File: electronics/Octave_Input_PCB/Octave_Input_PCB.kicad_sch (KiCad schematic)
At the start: 35 parts, among them SW1 SW_Hot_Swap_Socket, SW10 SW_Hot_Swap_Socket, SW11 SW_Hot_Swap_Socket, SW12 SW_Hot_Swap_Socket, SW13 Bourns_PEC12R-4xxxF-Sxxx, SW14 SW_Hot_Swap_Socket, SW2 SW_Hot_Swap_Socket, SW3 SW_Hot_Swap_Socket, SW4 SW_Hot_Swap_Socket, SW5 SW_Hot_Swap_Socket, SW6 SW_Hot_Swap_Socket, SW7 SW_Hot_Swap_Socket, SW8 SW_Hot_Swap_Socket, SW9 SW_Hot_Swap_Socket, U1 Adafruit_QT_Py_RP2040

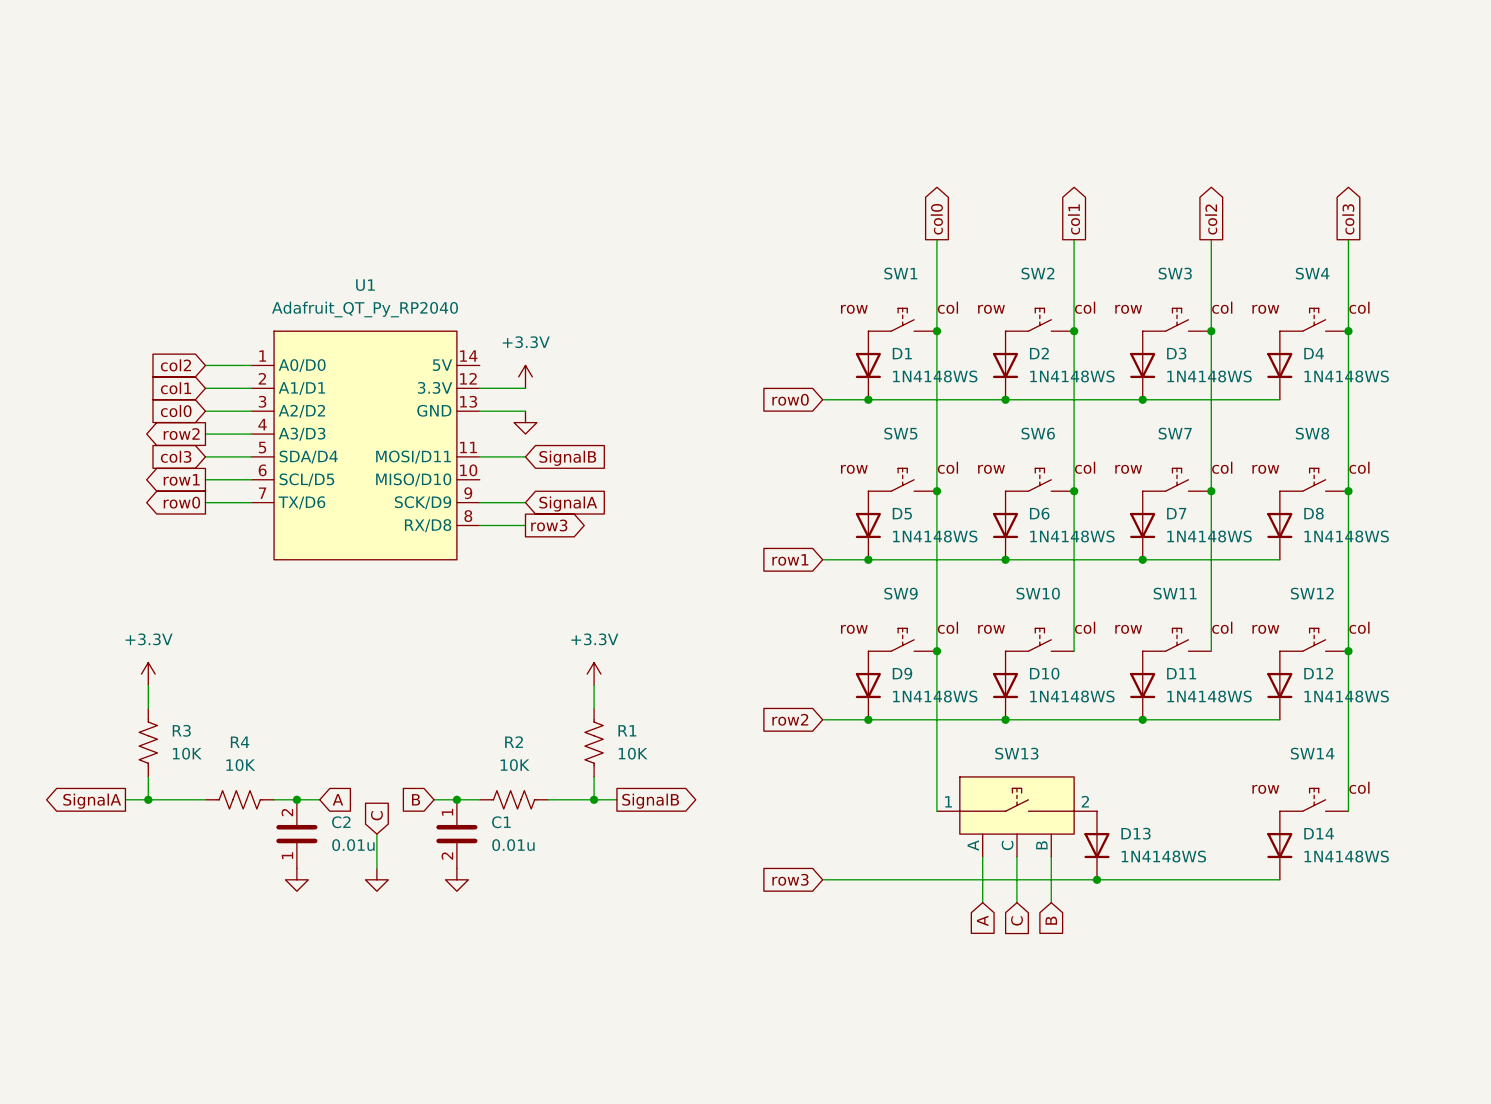
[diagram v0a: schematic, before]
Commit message: Schematic rev.1 is available
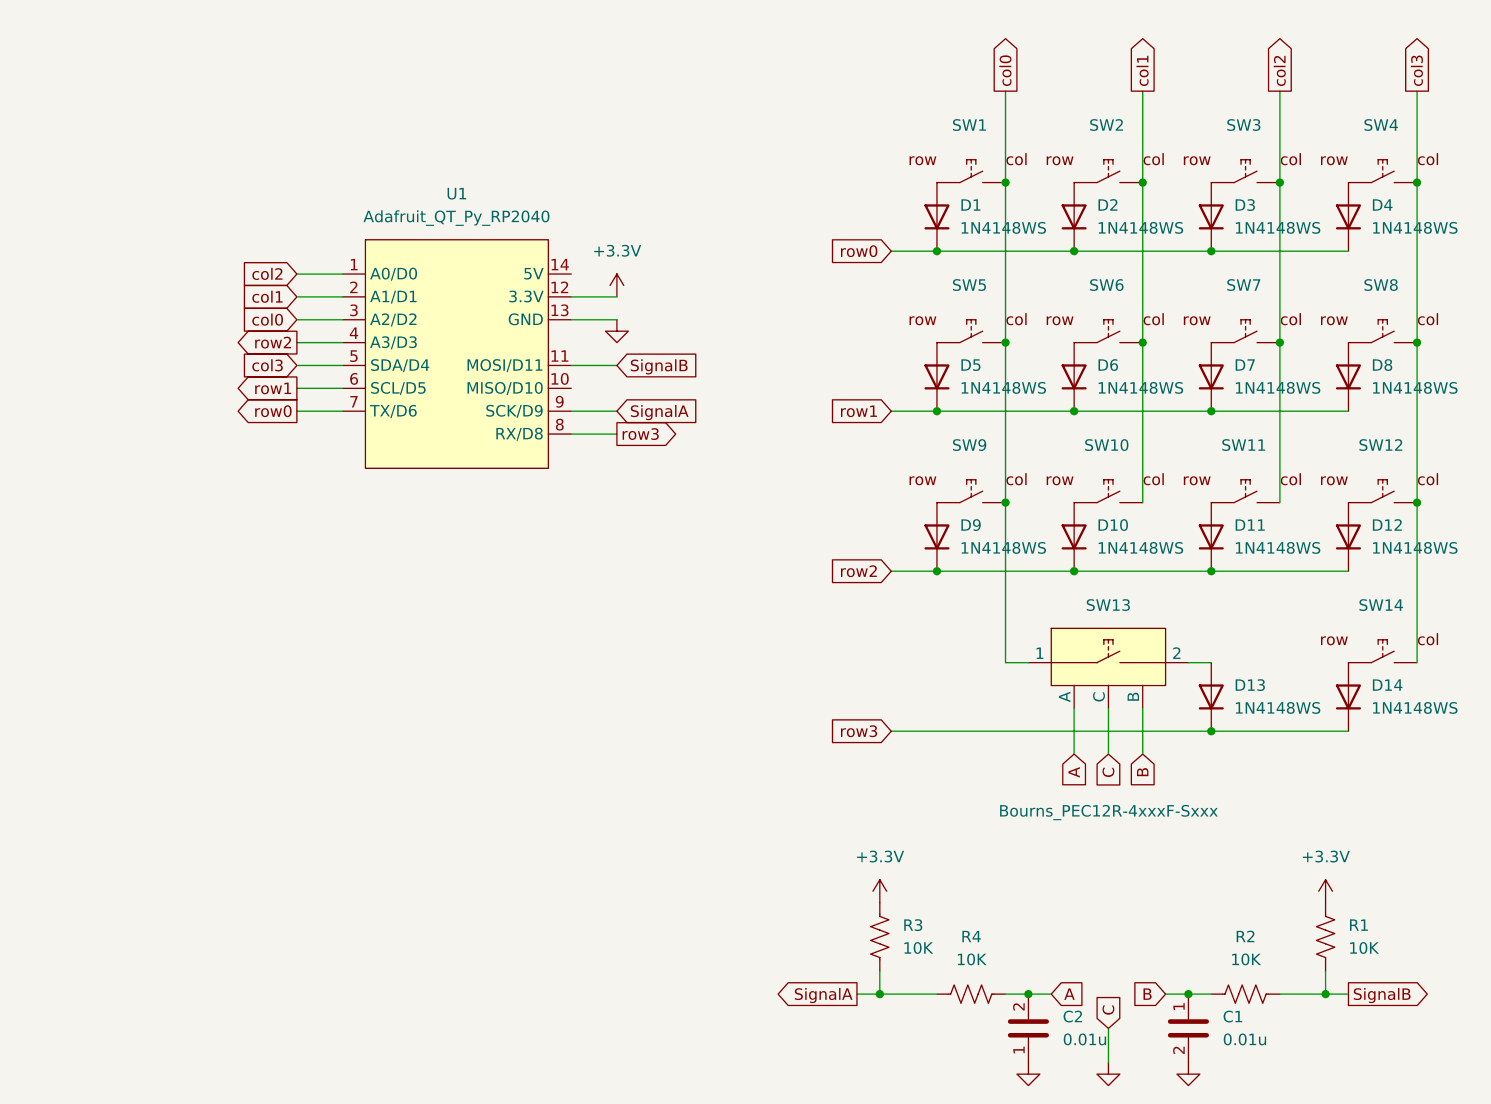
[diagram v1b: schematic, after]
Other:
- title: (none) -> Octave - Input PCB
- moved on the sheet: C1, C2, D1, D10, D11, D12, D13, D14, D2, D3, D4, D5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

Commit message: Reset PCB tracks
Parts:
- C1, C2: footprint Octave_Library:C_0805_2012Metric_Pad1.18x1.45mm_HandSolder -> Octave_Library:C_0805_2012Metric
- R1, R2, R3, R4: footprint Octave_Library:R_0805_2012Metric_Pad1.20x1.40mm_HandSolder -> Octave_Library:R_0805_2012Metric
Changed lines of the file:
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@@
       (effects (font (size 1.27 1.27)) (justify left))
     )
-    (property "Footprint" "Octave_Library:C_0805_2012Metric_Pad1.18x1.45mm_HandSolder" (id 2) (at 183.8452 143.51 0)
+    (property "Footprint" "Octave_Library:C_0805_2012Metric" (id 2) (at 183.8452 143.51 0)
       (effects (font (size 1.27 1.27)) hide)
     )
@@
       (effects (font (size 1.27 1.27)) (justify right))
     )
-    (property "Footprint" "Octave_Library:C_0805_2012Metric_Pad1.18x1.45mm_HandSolder" (id 2) (at 164.1348 135.89 0)
+    (property "Footprint" "Octave_Library:C_0805_2012Metric" (id 2) (at 164.1348 135.89 0)
       (effects (font (size 1.27 1.27)) hide)
     )
@@
     (property "Reference" "R2" (id 0) (at 189.23 129.54 90))
     (property "Value" "10K" (id 1) (at 189.23 132.08 90))
-    (property "Footprint" "Octave_Library:R_0805_2012Metric_Pad1.20x1.40mm_HandSolder" (id 2) (at 189.484 134.874 90)
+    (property "Footprint" "Octave_Library:R_0805_2012Metric" (id 2) (at 189.484 134.874 90)
       (effects (font (size 1.27 1.27)) hide)
     )
@@
     (property "Reference" "R4" (id 0) (at 158.75 129.54 90))
     (property "Value" "10K" (id 1) (at 158.75 132.08 90))
-    (property "Footprint" "Octave_Library:R_0805_2012Metric_Pad1.20x1.40mm_HandSolder" (id 2) (at 158.496 136.906 90)
+    (property "Footprint" "Octave_Library:R_0805_2012Metric" (id 2) (at 158.496 136.906 90)
       (effects (font (size 1.27 1.27)) hide)
     )
@@
       (effects (font (size 1.27 1.27)) (justify left))
     )
-    (property "Footprint" "Octave_Library:R_0805_2012Metric_Pad1.20x1.40mm_HandSolder" (id 2) (at 199.136 129.794 90)
+    (property "Footprint" "Octave_Library:R_0805_2012Metric" (id 2) (at 199.136 129.794 90)
       (effects (font (size 1.27 1.27)) hide)
     )
@@
       (effects (font (size 1.27 1.27)) (justify left))
     )
-    (property "Footprint" "Octave_Library:R_0805_2012Metric_Pad1.20x1.40mm_HandSolder" (id 2) (at 149.606 129.794 90)
+    (property "Footprint" "Octave_Library:R_0805_2012Metric" (id 2) (at 149.606 129.794 90)
       (effects (font (size 1.27 1.27)) hide)
     )
@@
     )
     (path "/172c53e1-ff21-4247-8ac3-d08b615ae4b5"
-      (reference "C1") (unit 1) (value "0.01u") (footprint "Octave_Library:C_0805_2012Metric_Pad1.18x1.45mm_HandSolder")
+      (reference "C1") (unit 1) (value "0.01u") (footprint "Octave_Library:C_0805_2012Metric")
     )
     (path "/21ad77bf-5ff1-4e47-a420-889e2c26128b"
-      (reference "C2") (unit 1) (value "0.01u") (footprint "Octave_Library:C_0805_2012Metric_Pad1.18x1.45mm_HandSolder")
+      (reference "C2") (unit 1) (value "0.01u") (footprint "Octave_Library:C_0805_2012Metric")
     )
     (path "/709f02fa-f113-4f34-aada-ad74ed9e0d25"
@@
     )
     (path "/64730bd7-54fc-4aec-9d2c-870b4ea1cdc7"
-      (reference "R1") (unit 1) (value "10K") (footprint "Octave_Library:R_0805_2012Metric_Pad1.20x1.40mm_HandSolder")
+      (reference "R1") (unit 1) (value "10K") (footprint "Octave_Library:R_0805_2012Metric")
     )
     (path "/21cf072e-e65a-4d3b-9444-6c6fd8351885"
-      (reference "R2") (unit 1) (value "10K") (footprint "Octave_Library:R_0805_2012Metric_Pad1.20x1.40mm_HandSolder")
+      (reference "R2") (unit 1) (value "10K") (footprint "Octave_Library:R_0805_2012Metric")
     )
     (path "/7d5f8a5b-f9ef-4146-ac71-a7ec0f7bb1c4"
-      (reference "R3") (unit 1) (value "10K") (footprint "Octave_Library:R_0805_2012Metric_Pad1.20x1.40mm_HandSolder")
+      (reference "R3") (unit 1) (value "10K") (footprint "Octave_Library:R_0805_2012Metric")
     )
     (path "/4c631ef9-ee73-4b0c-aa59-4f071756ed7f"
-      (reference "R4") (unit 1) (value "10K") (footprint "Octave_Library:R_0805_2012Metric_Pad1.20x1.40mm_HandSolder")
+      (reference "R4") (unit 1) (value "10K") (footprint "Octave_Library:R_0805_2012Metric")
     )
     (path "/ec285e65-9c46-4fa7-bf57-be16d5aaed04"

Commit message: Update schematic
Since label C hid GND in the net list, remove label C and simply connect to GND.
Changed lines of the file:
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@@
     (title "Octave - Input PCB")
     (date "2022-03-06")
-    (rev "1")
+    (rev "2")
     (comment 4 "https://github.com/takayoshiotake/octave-12-key-macropad")
   )
@@
   )
   (wire (pts (xy 193.04 63.5) (xy 193.04 81.28))
-    (stroke (width 0) (type default) (color 0 0 0 0))
-  )
-  (wire (pts (xy 173.99 139.7) (xy 173.99 143.51))
     (stroke (width 0) (type default) (color 0 0 0 0))
   )
@@
     )
   )
-  (global_label "C" (shape input) (at 173.99 139.7 90) (fields_autoplaced)
-    (effects (font (size 1.27 1.27)) (justify left))
-    (property "Intersheet References" "${INTERSHEET_REFS}" (id 0) (at 174.0694 136.0169 90)
-      (effects (font (size 1.27 1.27)) (justify left) hide)
-    )
-  )
   (global_label "SignalB" (shape output) (at 200.66 135.89 0) (fields_autoplaced)
     (effects (font (size 1.27 1.27)) (justify left))
@@
     (effects (font (size 1.27 1.27)) (justify right))
     (property "Intersheet References" "${INTERSHEET_REFS}" (id 0) (at 142.9717 71.0406 0)
-      (effects (font (size 1.27 1.27)) (justify right) hide)
-    )
-  )
-  (global_label "C" (shape input) (at 173.99 109.22 270) (fields_autoplaced)
-    (effects (font (size 1.27 1.27)) (justify right))
-    (property "Intersheet References" "${INTERSHEET_REFS}" (id 0) (at 173.9106 112.9031 90)
       (effects (font (size 1.27 1.27)) (justify right) hide)
     )
@@
     (pin "2")
   )
-  (symbol (lib_id "power:GND") (at 173.99 143.51 0) (unit 1)
-    (in_bom yes) (on_board yes) (fields_autoplaced)
-    (property "Reference" "#PWR05" (id 0) (at 173.99 149.86 0)
-      (effects (font (size 1.27 1.27)) hide)
-    )
-    (property "Value" "GND" (id 1) (at 173.99 148.59 0)
-      (effects (font (size 1.27 1.27)) hide)
-    )
-    (property "Footprint" "" (id 2) (at 173.99 143.51 0)
-      (effects (font (size 1.27 1.27)) hide)
-    )
-    (property "Datasheet" "" (id 3) (at 173.99 143.51 0)
-      (effects (font (size 1.27 1.27)) hide)
-    )
+  (symbol (lib_id "power:GND") (at 173.99 109.22 0) (unit 1)
+    (in_bom yes) (on_board yes) (fields_autoplaced)
+    (property "Reference" "#PWR05" (id 0) (at 173.99 115.57 0)
+      (effects (font (size 1.27 1.27)) hide)
+    )
+    (property "Value" "GND" (id 1) (at 173.99 114.3 0)
+      (effects (font (size 1.27 1.27)) hide)
+    )
+    (property "Footprint" "" (id 2) (at 173.99 109.22 0)
+      (effects (font (size 1.27 1.27)) hide)
+    )
+    (property "Datasheet" "" (id 3) (at 173.99 109.22 0)
+      (effects (font (size 1.27 1.27)) hide)
+    )

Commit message: Update schematic
Close some issues:
- Fix U1 symbol
- Change R1 and R3 value
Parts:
- R1, R3: value 10K -> 100K
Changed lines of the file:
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@@
   (title_block
     (title "Octave - Input PCB")
-    (date "2022-03-06")
-    (rev "2")
+    (date "2022-04-13")
+    (rev "3")
     (comment 4 "https://github.com/takayoshiotake/octave-12-key-macropad")
   )
@@
       (effects (font (size 1.27 1.27)) (justify left))
     )
-    (property "Value" "10K" (id 1) (at 200.66 130.8099 0)
+    (property "Value" "100K" (id 1) (at 200.66 130.8099 0)
       (effects (font (size 1.27 1.27)) (justify left))
     )
@@
       (effects (font (size 1.27 1.27)) (justify left))
     )
-    (property "Value" "10K" (id 1) (at 151.13 130.8099 0)
+    (property "Value" "100K" (id 1) (at 151.13 130.8099 0)
       (effects (font (size 1.27 1.27)) (justify left))
     )
@@
     )
     (path "/64730bd7-54fc-4aec-9d2c-870b4ea1cdc7"
-      (reference "R1") (unit 1) (value "10K") (footprint "Octave_Library:R_0805_2012Metric")
+      (reference "R1") (unit 1) (value "100K") (footprint "Octave_Library:R_0805_2012Metric")
     )
     (path "/21cf072e-e65a-4d3b-9444-6c6fd8351885"
@@
     )
     (path "/7d5f8a5b-f9ef-4146-ac71-a7ec0f7bb1c4"
-      (reference "R3") (unit 1) (value "10K") (footprint "Octave_Library:R_0805_2012Metric")
+      (reference "R3") (unit 1) (value "100K") (footprint "Octave_Library:R_0805_2012Metric")
     )
     (path "/4c631ef9-ee73-4b0c-aa59-4f071756ed7f"

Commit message: [WIP] Update schematic
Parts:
- added D14: 1N4148WS, Octave_Library:D_SOD-323, symbol Diode:1N4148WS
- added SW14: Alps_Alpine_RKJXV1224, Octave_Library:Stick_Controller_RKJXV122400R, symbol Octave_Library:Alps_Alpine_RKJXV1224
- renumbered D14 to D13, D13 to D15, SW14 to SW13, SW13 to SW15
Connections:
- net +3V3: now also SW14.3, SW14.6
- net GND: now also SW14.5, SW14.8
- net col0: now also SW13.2; no longer SW15.1
- net col2: now also SW14.2
- net col3: now also SW15.1; no longer SW13.2
- net row3: now also D14.1 (K)
- new net: D14.2 (A), SW14.1
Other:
- moved on the sheet: C1, C2, D1, D10, D11, D12, D13, D15, D2, D3, D4, D5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
